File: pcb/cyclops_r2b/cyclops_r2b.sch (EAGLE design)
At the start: 52 parts, among them IC2 317, IC3 REF02Z, IC5 LM324N

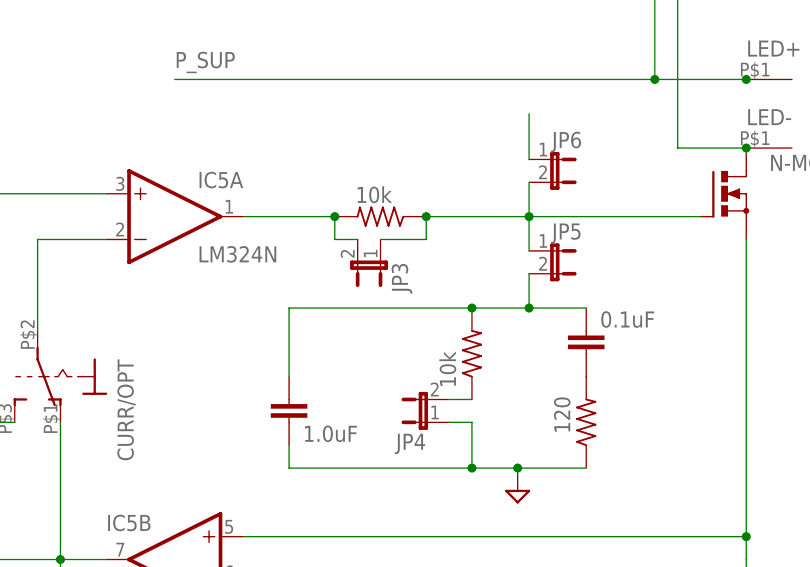
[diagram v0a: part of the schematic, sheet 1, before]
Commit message: Changed filter network resistor values to 0R to indicate application dependence.
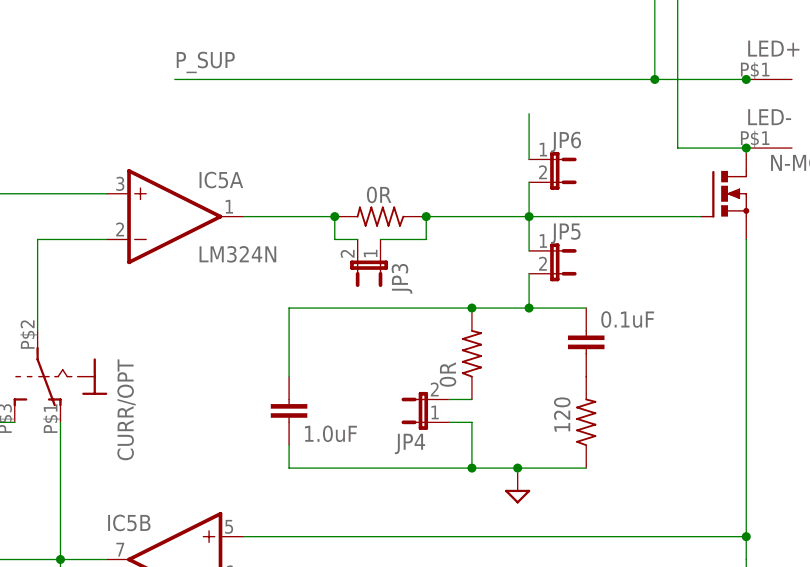
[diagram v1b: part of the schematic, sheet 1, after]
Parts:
- R3, R4: value 10k -> 0R
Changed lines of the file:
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@@
 <part name="V_AUX" library="con-coax" deviceset="?227161*" device="1-" technology="-0"/>
 <part name="SUPPLY3" library="supply2" deviceset="GND" device=""/>
-<part name="R3" library="HOSS" deviceset="R-US_" device="0207/7" value="10k"/>
-<part name="R4" library="HOSS" deviceset="R-US_" device="0207/7" value="10k"/>
+<part name="R3" library="HOSS" deviceset="R-US_" device="0207/7" value="0R"/>
+<part name="R4" library="HOSS" deviceset="R-US_" device="0207/7" value="0R"/>
 <part name="JP3" library="jumper" deviceset="JP1E" device=""/>
 <part name="JP2" library="jumper" deviceset="JP3Q" device=""/>

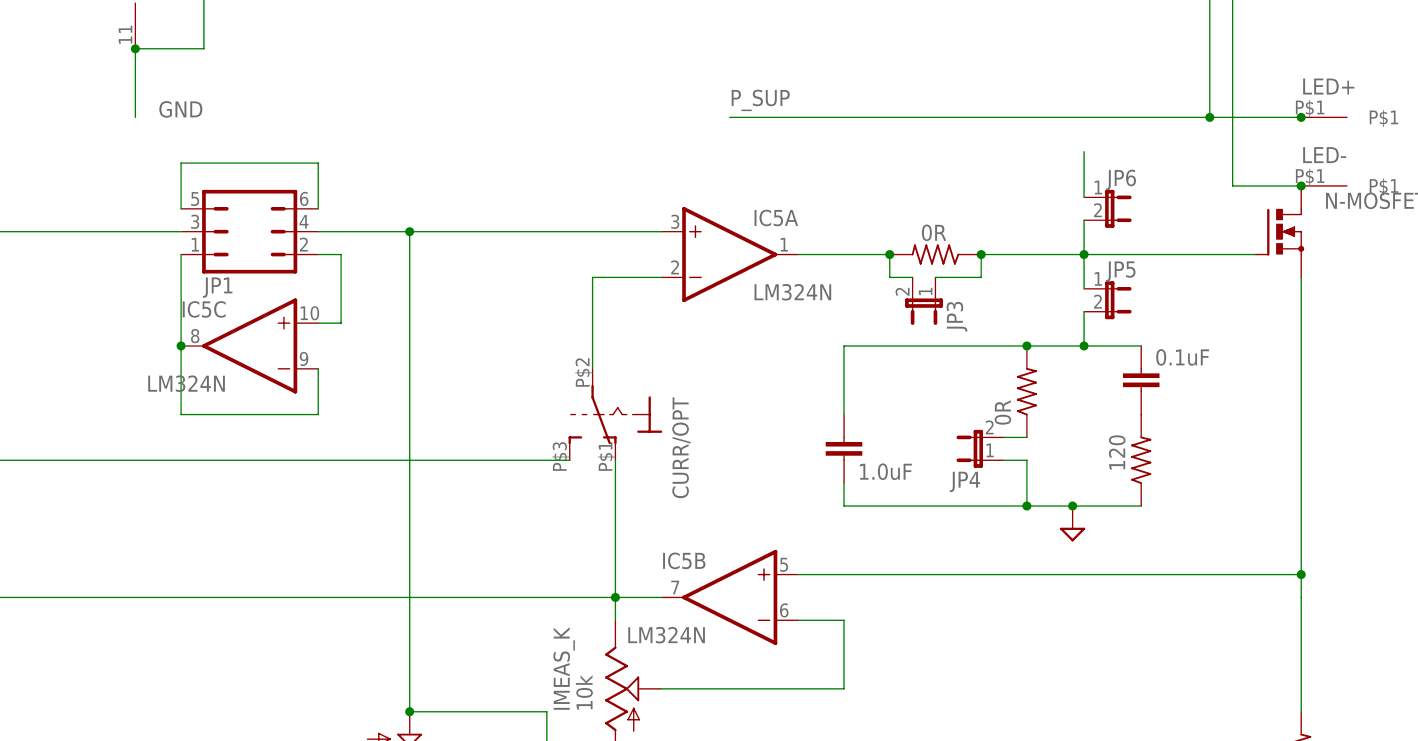
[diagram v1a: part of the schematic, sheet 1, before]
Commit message: Fixed r2b in terms of extra traces, ground plane islands, and added extra tuning resistor that was available in r0, but was removed in r2.
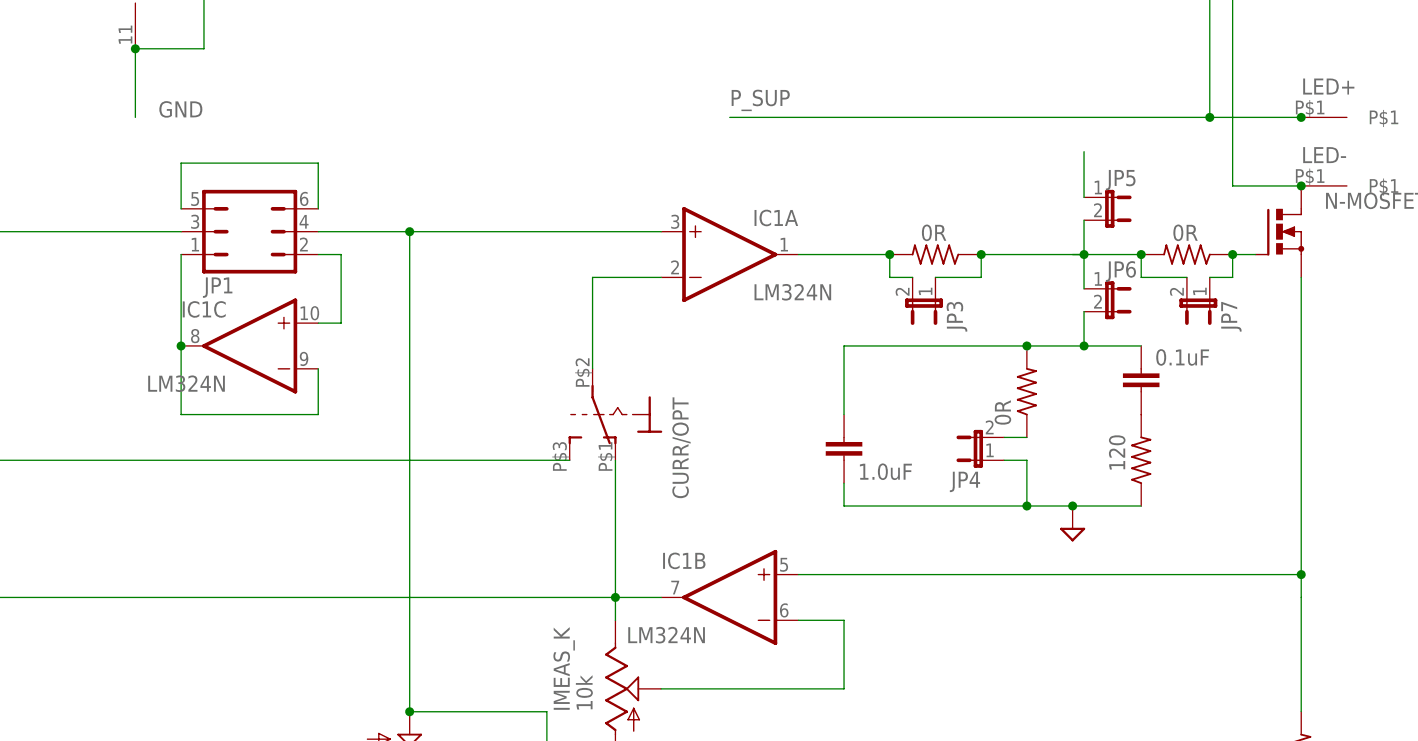
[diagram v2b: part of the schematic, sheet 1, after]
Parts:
- removed C8: 10u, rcl:C-EU025-024X044
- removed R9: 1k, HOSS:R-US_0207/7
- added C1: 0.1uF, rcl:C-EU050-024X044
- added JP7: (no value), jumper:JP1E
- added R1: 0R, HOSS:R-US_0207/7
- added R6: 1.5k, HOSS:R-US_0207/7
- C2: value 0.1uF -> 1.0uF; device rcl:C-EU050-024X044 -> rcl:C-EU025-024X044
- C3: value 1.0uF -> 0.1uF; device rcl:C-EU025-024X044 -> rcl:C-EU050-024X044
- C7: value 0.1uF -> 10u; device rcl:C-EU050-024X044 -> rcl:C-EU025-024X044
- POW1: value (none) -> SCREW2; device jumper:JP2Q -> HOSS:SCREW2
- POW2: value SCREW2 -> (none); device HOSS:SCREW2 -> jumper:JP2Q
- R2: value 1.5k -> 0R
- R3: value 0R -> 120
- R8: value 120 -> 1k
- renumbered IC5 to IC1, R10 to R5, R12 to R7
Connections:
- new net N$16: JP7.2, R4.2
- new net N$30: JP7.1, N-MOSFET.G, R4.1
- net GND: now also C1.2, C2.2, C7.1, POW1.P$1, POW2.4, R3.1, R8.2; no longer C3.2, C7.2, C8.1, POW1.4, POW2.P$1, R8.1, R9.2
- net N$11: now also JP6.2, R2.2; no longer JP5.2, R3.2
- net N$13: now also C3.2, R3.2; no longer C2.2, R8.2
- net N$24: now also R8.1; no longer R9.1
- net N$27: now also R2.1; no longer R3.1
- net N$28: now also R6.1; no longer R2.1
- net N$29: now also JP5.2, JP6.1, R1.1; no longer JP5.1, JP6.2, N-MOSFET.G, R4.1
- net N$3: now also R1.2; no longer R4.2
- net N$69: now also JP5.1; no longer JP6.1
- net P_12V: now also C1.1, R6.2; no longer C7.1, R2.2
- net P_SUP: now also C7.2; no longer C8.2
- net P_SUP_BEFORE: now also POW1.P$2, POW2.1; no longer POW1.1, POW2.P$2
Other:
- moved on the sheet: JP5, JP6

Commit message: Finished revision 2b. Sent for fabrication.
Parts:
- IC3: value REF02Z -> REF02; device linear:REF02Z -> linear:REF02DIL08-LONG
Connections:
- net GND: now also V_AUX.2, V_CTL.2, V_CURR.2, V_REF.2; no longer V_AUX.GND, V_CTL.GND, V_CURR.GND, V_REF.GND
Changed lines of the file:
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@@
 <part name="TP_5V" library="testpad" deviceset="TP" device="PAD1-13"/>
 <part name="JP5" library="jumper" deviceset="JP1E" device=""/>
-<part name="IC3" library="linear" deviceset="REF02" device="Z"/>
+<part name="IC3" library="linear" deviceset="REF02" device="DIL08-LONG" value="REF02"/>
 <part name="REG_ADJ" library="HOSS" deviceset="TRIM_US-" device="RJ6S" value="5k"/>
 <part name="REF_ADJ" library="HOSS" deviceset="TRIM_US-" device="RJ6S" value="10k"/>
@@
 <junction x="-66.04" y="73.66"/>
 <pinref part="SUPPLY3" gate="GND" pin="GND"/>
-<pinref part="V_CTL" gate="G$1" pin="GND"/>
-<pinref part="V_REF" gate="G$1" pin="GND"/>
-<pinref part="V_AUX" gate="G$1" pin="GND"/>
-<pinref part="V_CURR" gate="G$1" pin="GND"/>
+<pinref part="V_CTL" gate="G$1" pin="2"/>
+<pinref part="V_REF" gate="G$1" pin="2"/>
+<pinref part="V_AUX" gate="G$1" pin="2"/>
+<pinref part="V_CURR" gate="G$1" pin="2"/>
 <pinref part="I/O_BLOCK" gate="G$1" pin="P$1"/>
 </segment>

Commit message: Fixed several problems with r2b.
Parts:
- +12V, GND1, GND2, LED+, LED-, V_IN1: device HOSS:BANANA_TO_BOARD -> cyclops:BANANA_TO_BOARD
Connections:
- removed net N$16: JP7.2, R4.2
- net N$29: now also JP7.2, R4.2
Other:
- moved on the sheet: +12V, GND1, GND2, LED+, LED-, V_IN1
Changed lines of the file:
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@@
 <setting verticaltext="up"/>
 </settings>
-<grid distance="0.1" unitdist="inch" unit="inch" style="lines" multiple="1" display="no" altdistance="0.01" altunitdist="inch" altunit="inch"/>
+<grid distance="0.05" unitdist="inch" unit="inch" style="lines" multiple="1" display="no" altdistance="0.01" altunitdist="inch" altunit="inch"/>
 <layers>
 <layer number="1" name="Top" color="4" fill="1" visible="no" active="no"/>
@@
 <part name="IMEAS_K" library="HOSS" deviceset="TRIM_US-" device="RJ6S" value="10k"/>
 <part name="CTL_K" library="HOSS" deviceset="TRIM_US-" device="RJ6S" value="10k"/>
-<part name="LED+" library="HOSS" deviceset="BANANA_TO_BOARD" device=""/>
-<part name="LED-" library="HOSS" deviceset="BANANA_TO_BOARD" device=""/>
+<part name="LED+" library="cyclops" deviceset="BANANA_TO_BOARD" device=""/>
+<part name="LED-" library="cyclops" deviceset="BANANA_TO_BOARD" device=""/>
 <part name="JP1" library="jumper" deviceset="JP3Q" device=""/>
 <part name="C1" library="rcl" deviceset="C-EU" device="050-024X044" value="0.1uF"/>
@@
 <part name="R7" library="HOSS" deviceset="R-US_" device="0207/7" value="470"/>
 <part name="SUPPLY6" library="supply2" deviceset="GND" device=""/>
-<part name="+12V" library="HOSS" deviceset="BANANA_TO_BOARD" device=""/>
-<part name="GND1" library="HOSS" deviceset="BANANA_TO_BOARD" device=""/>
+<part name="+12V" library="cyclops" deviceset="BANANA_TO_BOARD" device=""/>
+<part name="GND1" library="cyclops" deviceset="BANANA_TO_BOARD" device=""/>
 <part name="IC2" library="HOSS" deviceset="*317" device=""/>
 <part name="R6" library="HOSS" deviceset="R-US_" device="0207/7" value="1.5k"/>
@@
 <part name="MECH2" library="jumper" deviceset="JP2Q" device=""/>
 <part name="SUPPLY7" library="supply2" deviceset="GND" device=""/>
-<part name="V_IN1" library="HOSS" deviceset="BANANA_TO_BOARD" device=""/>
-<part name="GND2" library="HOSS" deviceset="BANANA_TO_BOARD" device=""/>
+<part name="V_IN1" library="cyclops" deviceset="BANANA_TO_BOARD" device=""/>
+<part name="GND2" library="cyclops" deviceset="BANANA_TO_BOARD" device=""/>
 <part name="POW1" library="HOSS" deviceset="SCREW2" device=""/>
 <part name="C7" library="rcl" deviceset="C-EU" device="025-024X044" value="10u"/>
@@
 <wire x1="83.82" y1="81.28" x2="83.82" y2="83.82" width="0.1524" layer="91"/>
 <wire x1="78.74" y1="81.28" x2="83.82" y2="81.28" width="0.1524" layer="91"/>
-<wire x1="95.25" y1="83.82" x2="95.25" y2="80.01" width="0.1524" layer="91"/>
 <wire x1="83.82" y1="83.82" x2="95.25" y2="83.82" width="0.1524" layer="91"/>
-<wire x1="95.25" y1="83.82" x2="95.25" y2="87.63" width="0.1524" layer="91"/>
 <junction x="83.82" y="83.82"/>
-<junction x="95.25" y="83.82"/>
 <pinref part="R1" gate="G$1" pin="1"/>
 <pinref part="JP3" gate="A" pin="1"/>
+<wire x1="95.25" y1="83.82" x2="101.6" y2="83.82" width="0.1524" layer="91"/>
+<wire x1="106.68" y1="81.28" x2="101.6" y2="81.28" width="0.1524" layer="91"/>
+<wire x1="101.6" y1="81.28" x2="101.6" y2="83.82" width="0.1524" layer="91"/>
+<pinref part="R4" gate="G$1" pin="2"/>
+<pinref part="JP7" gate="A" pin="2"/>
+<junction x="101.6" y="83.82"/>
+<pinref part="JP5" gate="A" pin="2"/>
+<wire x1="95.25" y1="80.01" x2="95.25" y2="83.82" width="0.1524" layer="91"/>
 <pinref part="JP6" gate="A" pin="1"/>
-<pinref part="JP5" gate="A" pin="2"/>
+<junction x="95.25" y="83.82"/>
+<wire x1="95.25" y1="83.82" x2="95.25" y2="87.63" width="0.1524" layer="91"/>
 </segment>
 </net>
@@
 </segment>
 </net>
-<net name="N$16" class="0">
-<segment>
-<wire x1="93.98" y1="83.82" x2="101.6" y2="83.82" width="0.1524" layer="91"/>
-<wire x1="106.68" y1="81.28" x2="101.6" y2="81.28" width="0.1524" layer="91"/>
-<wire x1="101.6" y1="81.28" x2="101.6" y2="83.82" width="0.1524" layer="91"/>
-<junction x="101.6" y="83.82"/>
-<pinref part="R4" gate="G$1" pin="2"/>
-<pinref part="JP7" gate="A" pin="2"/>
-</segment>
-</net>

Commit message: Ready for printing.
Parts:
- V_AUX, V_CTL, V_CURR, V_REF: device con-coax:1-227161-0 -> cyclops:1-227161-0
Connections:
- net GND: now also V_AUX.GND, V_CTL.GND, V_CURR.GND, V_REF.GND; no longer V_AUX.2, V_CTL.2, V_CURR.2, V_REF.2
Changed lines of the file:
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@@
 <setting verticaltext="up"/>
 </settings>
-<grid distance="0.05" unitdist="inch" unit="inch" style="lines" multiple="1" display="no" altdistance="0.01" altunitdist="inch" altunit="inch"/>
+<grid distance="0.1" unitdist="inch" unit="inch" style="lines" multiple="1" display="no" altdistance="0.01" altunitdist="inch" altunit="inch"/>
 <layers>
 <layer number="1" name="Top" color="4" fill="1" visible="no" active="no"/>
@@
 <part name="R3" library="HOSS" deviceset="R-US_" device="0207/7" value="120"/>
 <part name="C2" library="rcl" deviceset="C-EU" device="025-024X044" value="1.0uF"/>
-<part name="V_CURR" library="con-coax" deviceset="?227161*" device="1-" technology="-0"/>
-<part name="V_CTL" library="con-coax" deviceset="?227161*" device="1-" technology="-0"/>
+<part name="V_CURR" library="cyclops" deviceset="?227161*" device="1-" technology="-0"/>
+<part name="V_CTL" library="cyclops" deviceset="?227161*" device="1-" technology="-0"/>
 <part name="IC1" library="linear" deviceset="LM324" device="N"/>
-<part name="V_REF" library="con-coax" deviceset="?227161*" device="1-" technology="-0"/>
-<part name="V_AUX" library="con-coax" deviceset="?227161*" device="1-" technology="-0"/>
+<part name="V_REF" library="cyclops" deviceset="?227161*" device="1-" technology="-0"/>
+<part name="V_AUX" library="cyclops" deviceset="?227161*" device="1-" technology="-0"/>
 <part name="SUPPLY3" library="supply2" deviceset="GND" device=""/>
 <part name="R2" library="HOSS" deviceset="R-US_" device="0207/7" value="0R"/>
@@
 <junction x="-66.04" y="73.66"/>
 <pinref part="SUPPLY3" gate="GND" pin="GND"/>
-<pinref part="V_CTL" gate="G$1" pin="2"/>
-<pinref part="V_REF" gate="G$1" pin="2"/>
-<pinref part="V_AUX" gate="G$1" pin="2"/>
-<pinref part="V_CURR" gate="G$1" pin="2"/>
+<pinref part="V_CTL" gate="G$1" pin="GND"/>
+<pinref part="V_REF" gate="G$1" pin="GND"/>
+<pinref part="V_AUX" gate="G$1" pin="GND"/>
+<pinref part="V_CURR" gate="G$1" pin="GND"/>
 <pinref part="I/O_BLOCK" gate="G$1" pin="P$1"/>
 </segment>
